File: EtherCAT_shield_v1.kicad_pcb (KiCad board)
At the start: 2 copper layers, 73.7 x 81.3 mm, 69 parts, among them J1 RJ45-PULSETRANS, J2 RJ45-PULSETRANS, P1 CONN_02X10, P2 CONN_02X19, P3 CONN_02X19, U1 LAN9252, U2 24LC00, Y1 Crystal_GND24

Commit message: ロゴ追加した
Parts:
- added G***: LOGO, EtherCAT_Logo:EtherCAT_900dpi, F.Cu at (102.0, 65.0)
- moved D1 11.7 mm to (109.8, 74.0)
- moved D2 11.7 mm to (109.8, 77.0)
- moved R1 11.7 mm to (106.8, 74.0)
- moved R2 11.7 mm to (106.8, 77.0)

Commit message: 進捗
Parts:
- U2: footprint Housings_SOIC:SOIC-8_3.9x4.9mm_Pitch1.27mm -> Housings_DIP:DIP-8_W7.62mm_Socket_LongPads
- moved C6 48.7 mm to (137.4, 91.2), turned to 270 degrees
- moved C7 44.7 mm to (140.0, 86.2)
- moved C10 20.0 mm to (162.3, 71.4)
- moved C8 20.0 mm to (162.3, 74.2)
- moved C9 20.0 mm to (162.3, 72.8)
- moved C25 11.6 mm to (145.9, 78.9), turned to 0 degrees
- moved C12 11.6 mm to (133.8, 94.8)
- moved C13 11.6 mm to (136.7, 93.5)
- moved C14 11.6 mm to (133.8, 93.5)
- moved C15 11.6 mm to (136.7, 94.8)
- moved U2 10.7 mm to (144.6, 89.0), turned to 90 degrees
- moved R22 10.4 mm to (153.7, 72.2), turned to 90 degrees
- moved R24 9.55 mm to (149.0, 72.0), turned to 270 degrees
- moved R23 9.36 mm to (155.3, 72.2), turned to 90 degrees
- moved R19 9.31 mm to (150.2, 78.4), turned to 270 degrees
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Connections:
- J1 pad 11: Net-(J1-Pad11) -> (no net)
- J1 pad 12: Net-(J1-Pad12) -> (no net)
- J1 pad 13: GND -> GNDPWR
- J1 pad 14: GND -> GNDPWR
- J1 pad 8: GND -> GNDPWR
- J2 pad 11: Net-(J2-Pad11) -> (no net)
- J2 pad 12: Net-(J2-Pad12) -> (no net)
- J2 pad 13: GND -> GNDPWR
- J2 pad 14: GND -> GNDPWR
- J2 pad 8: GND -> GNDPWR
- P2 pad 10: Net-(P2-Pad10) -> (no net)
- P2 pad 11: Net-(P2-Pad11) -> (no net)
- P2 pad 13: Net-(P2-Pad13) -> (no net)
- P2 pad 14: Net-(P2-Pad14) -> (no net)
- P2 pad 15: Net-(P2-Pad15) -> (no net)
- P2 pad 17: Net-(P2-Pad17) -> (no net)
- P2 pad 18: Net-(P2-Pad18) -> (no net)
- P2 pad 2: Net-(P2-Pad2) -> (no net)
- P2 pad 21: Net-(P2-Pad21) -> (no net)
- P2 pad 23: Net-(P2-Pad23) -> (no net)
- P2 pad 24: Net-(P2-Pad24) -> (no net)
- P2 pad 25: Net-(P2-Pad25) -> (no net)
- P2 pad 26: Net-(P2-Pad26) -> (no net)
- P2 pad 27: Net-(P2-Pad27) -> (no net)
- P2 pad 28: Net-(P2-Pad28) -> (no net)
- P2 pad 29: Net-(P2-Pad29) -> (no net)
- P2 pad 3: Net-(P2-Pad3) -> (no net)
- P2 pad 30: Net-(P2-Pad30) -> (no net)
- P2 pad 31: Net-(P2-Pad31) -> (no net)
- P2 pad 32: Net-(P2-Pad32) -> (no net)
- P2 pad 33: Net-(P2-Pad33) -> (no net)
- P2 pad 34: Net-(P2-Pad34) -> (no net)
- P2 pad 35: Net-(P2-Pad35) -> (no net)
- P2 pad 36: Net-(P2-Pad36) -> (no net)
- P2 pad 37: Net-(P2-Pad37) -> (no net)
- P2 pad 38: Net-(P2-Pad38) -> (no net)
- P2 pad 4: Net-(P2-Pad4) -> (no net)
- P2 pad 5: Net-(P2-Pad5) -> (no net)
- P2 pad 6: Net-(P2-Pad6) -> (no net)
- P2 pad 7: Net-(P2-Pad7) -> (no net)
- P2 pad 9: Net-(P2-Pad9) -> (no net)
- P3 pad 10: Net-(P3-Pad10) -> (no net)
- P3 pad 11: Net-(P3-Pad11) -> (no net)
- P3 pad 12: Net-(P3-Pad12) -> (no net)
- P3 pad 13: Net-(P3-Pad13) -> (no net)
- P3 pad 14: Net-(P3-Pad14) -> (no net)
- P3 pad 15: Net-(P3-Pad15) -> (no net)
- P3 pad 16: Net-(P3-Pad16) -> (no net)
- P3 pad 18: Net-(P3-Pad18) -> (no net)
- P3 pad 19: Net-(P3-Pad19) -> (no net)
- P3 pad 2: Net-(P3-Pad2) -> (no net)
- P3 pad 21: Net-(P3-Pad21) -> (no net)
- P3 pad 23: Net-(P3-Pad23) -> (no net)
- P3 pad 24: Net-(P3-Pad24) -> (no net)
- P3 pad 25: Net-(P3-Pad25) -> (no net)
- P3 pad 26: Net-(P3-Pad26) -> (no net)
- P3 pad 27: Net-(P3-Pad27) -> (no net)
- P3 pad 28: Net-(P3-Pad28) -> (no net)
- P3 pad 29: Net-(P3-Pad29) -> (no net)
- P3 pad 3: Net-(P3-Pad3) -> (no net)
- P3 pad 30: Net-(P3-Pad30) -> (no net)
- P3 pad 31: Net-(P3-Pad31) -> (no net)
- P3 pad 33: Net-(P3-Pad33) -> (no net)
- P3 pad 34: Net-(P3-Pad34) -> (no net)
- P3 pad 35: Net-(P3-Pad35) -> (no net)
- P3 pad 36: Net-(P3-Pad36) -> (no net)
- P3 pad 37: Net-(P3-Pad37) -> (no net)
- P3 pad 38: Net-(P3-Pad38) -> (no net)
- P3 pad 4: Net-(P3-Pad4) -> (no net)
- P3 pad 5: Net-(P3-Pad5) -> (no net)
- P3 pad 6: Net-(P3-Pad6) -> (no net)
- P3 pad 7: Net-(P3-Pad7) -> (no net)
- P3 pad 8: Net-(P3-Pad8) -> (no net)
- R23 pad 2: Net-(D3-Pad1) -> +3V3
- U1 pad 12: Net-(U1-Pad12) -> (no net)
- U1 pad 18: Net-(U1-Pad18) -> (no net)
- U1 pad 25: Net-(U1-Pad25) -> (no net)
- U1 pad 3: Net-(U1-Pad3) -> (no net)
- U1 pad 34: Net-(U1-Pad34) -> (no net)
- U1 pad 35: Net-(U1-Pad35) -> (no net)
- U1 pad 44: /LAN9252/IRQ -> (no net)
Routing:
- net Net-(P1-Pad9): track 2.25 -> 55.5 mm, vias 1 -> 2
- net +3V3: track 0.00 -> 52.8 mm, vias 0 -> 2
- net GNDPWR: track 0.00 -> 51.9 mm
- net Net-(P1-Pad7): track 0.00 -> 51.3 mm, vias 0 -> 1
- net Net-(P1-Pad5): track 0.00 -> 48.7 mm, vias 0 -> 1
- net Net-(P1-Pad16): track 0.00 -> 47.0 mm, vias 0 -> 1
- net Net-(P1-Pad3): track 0.00 -> 45.1 mm
- net Net-(P1-Pad17): track 0.00 -> 44.2 mm
- net Net-(P1-Pad15): track 0.00 -> 43.7 mm
- net Net-(P1-Pad13): track 0.00 -> 42.7 mm
- net Net-(P1-Pad4): track 0.00 -> 41.9 mm, vias 0 -> 1
- net Net-(P1-Pad11): track 0.00 -> 41.8 mm, vias 0 -> 1
- net Net-(P1-Pad14): track 0.00 -> 40.6 mm
- net Net-(P1-Pad6): track 0.00 -> 39.6 mm
- net Net-(P1-Pad8): track 0.00 -> 39.1 mm, vias 0 -> 1
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- added copper zone on B.Cu, net GND
- added copper zone on F.Cu, net GND

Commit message: 進捗
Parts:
- C5, C6, C7, C8, C9, R18: moved to B.Cu
- moved C10 37.4 mm to (126.5, 82.2), turned to 90 degrees
- moved C9 36.8 mm to (128.4, 87.2)
- moved C8 34.7 mm to (131.1, 89.4), turned to 90 degrees
- moved C12 13.2 mm to (129.9, 82.2), turned to 90 degrees
- moved C14 12.4 mm to (128.5, 82.2), turned to 90 degrees
- moved C15 9.71 mm to (138.1, 85.2), turned to 180 degrees
- moved R21 9.11 mm to (123.4, 83.8), turned to 90 degrees
- moved R12 7.50 mm to (125.0, 83.8), turned to 90 degrees
- moved C1 6.91 mm to (121.9, 83.8), turned to 90 degrees
- moved C13 5.73 mm to (132.6, 89.4), turned to 90 degrees
- moved R4 5.53 mm to (120.4, 83.8), turned to 270 degrees
- moved R2 3.15 mm to (108.6, 75.5), turned to 0 degrees
- moved R1 3.05 mm to (108.6, 72.5), turned to 0 degrees
- moved R18 3.01 mm to (128.1, 84.4), turned to 0 degrees
- moved D2 2.95 mm to (111.6, 75.5), turned to 180 degrees
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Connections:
- P2 pad 21: (no net) -> /LAN9252/IRQ
- P2 pad 23: (no net) -> /LAN9252/~RST
- P2 pad 25: (no net) -> Net-(P2-Pad25)
- P2 pad 27: (no net) -> Net-(P2-Pad27)
- P2 pad 6: (no net) -> +5V
- U1 pad 18: (no net) -> Net-(P2-Pad27)
- U1 pad 34: (no net) -> Net-(P2-Pad25)
- U1 pad 44: (no net) -> /LAN9252/IRQ
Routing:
- net GND: track 143.2 -> 299.6 mm, vias 16 -> 33
- net +3V3: track 52.8 -> 186.8 mm, vias 2 -> 9
- net /LAN9252/IRQ: track 0.00 -> 63.3 mm, vias 0 -> 1
- net /LAN9252/~RST: track 0.00 -> 55.0 mm, vias 0 -> 1
- net Net-(P2-Pad27): track 0.00 -> 44.2 mm, vias 0 -> 2
- net Net-(P1-Pad16): track 47.0 -> 3.96 mm, vias 1 -> 0
- net Net-(P1-Pad4): track 41.9 -> 3.47 mm, vias 1 -> 0
- net Net-(P3-Pad17): track 3.35 -> 41.4 mm
- net Net-(C12-Pad1): track 0.00 -> 37.4 mm, vias 0 -> 3
- net Net-(P1-Pad14): track 40.6 -> 3.26 mm
- net Net-(P1-Pad6): track 39.6 -> 3.49 mm
- net Net-(P1-Pad8): track 39.1 -> 3.53 mm, vias 1 -> 0
- net Net-(P1-Pad12): track 39.0 -> 3.69 mm, vias 1 -> 0
- net Net-(P1-Pad10): track 38.4 -> 4.15 mm, vias 1 -> 0
- net Net-(P1-Pad3): track 45.1 -> 10.9 mm
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
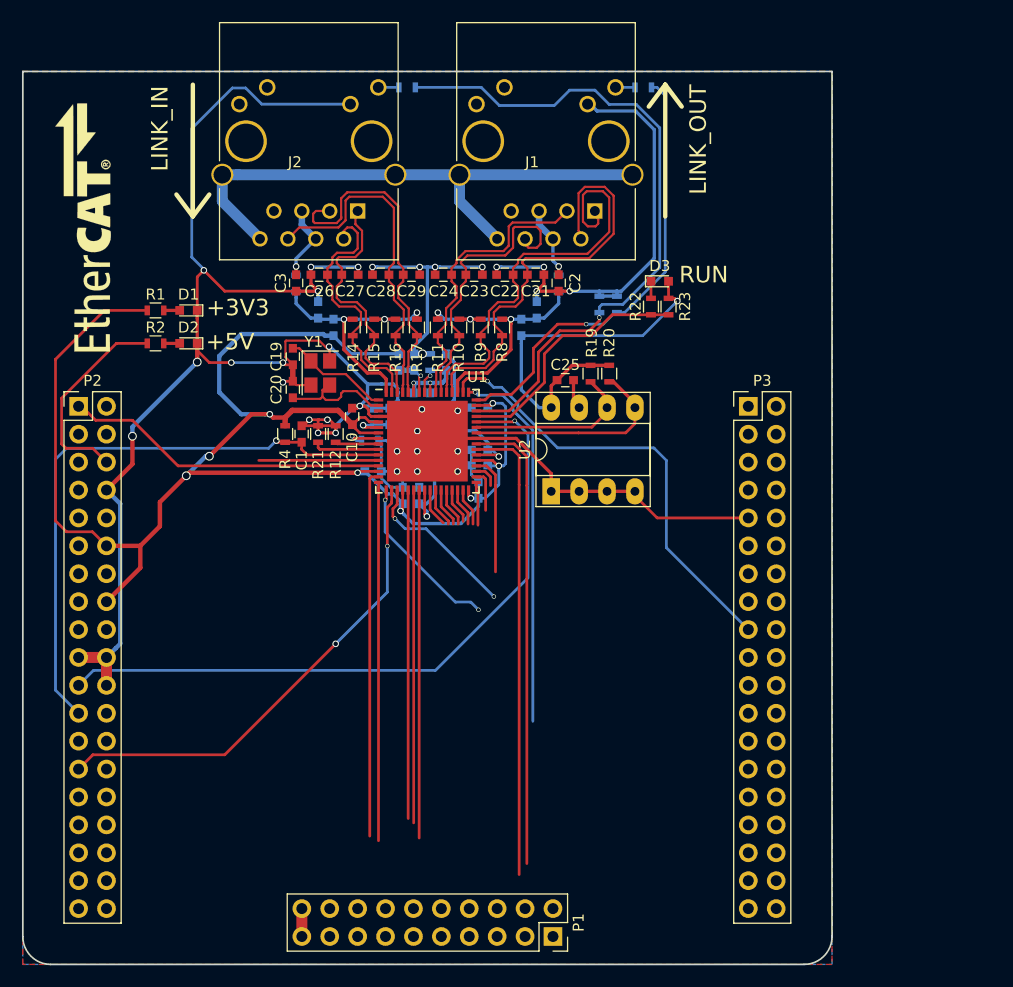
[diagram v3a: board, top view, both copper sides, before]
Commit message: LED変更，再アノテーション
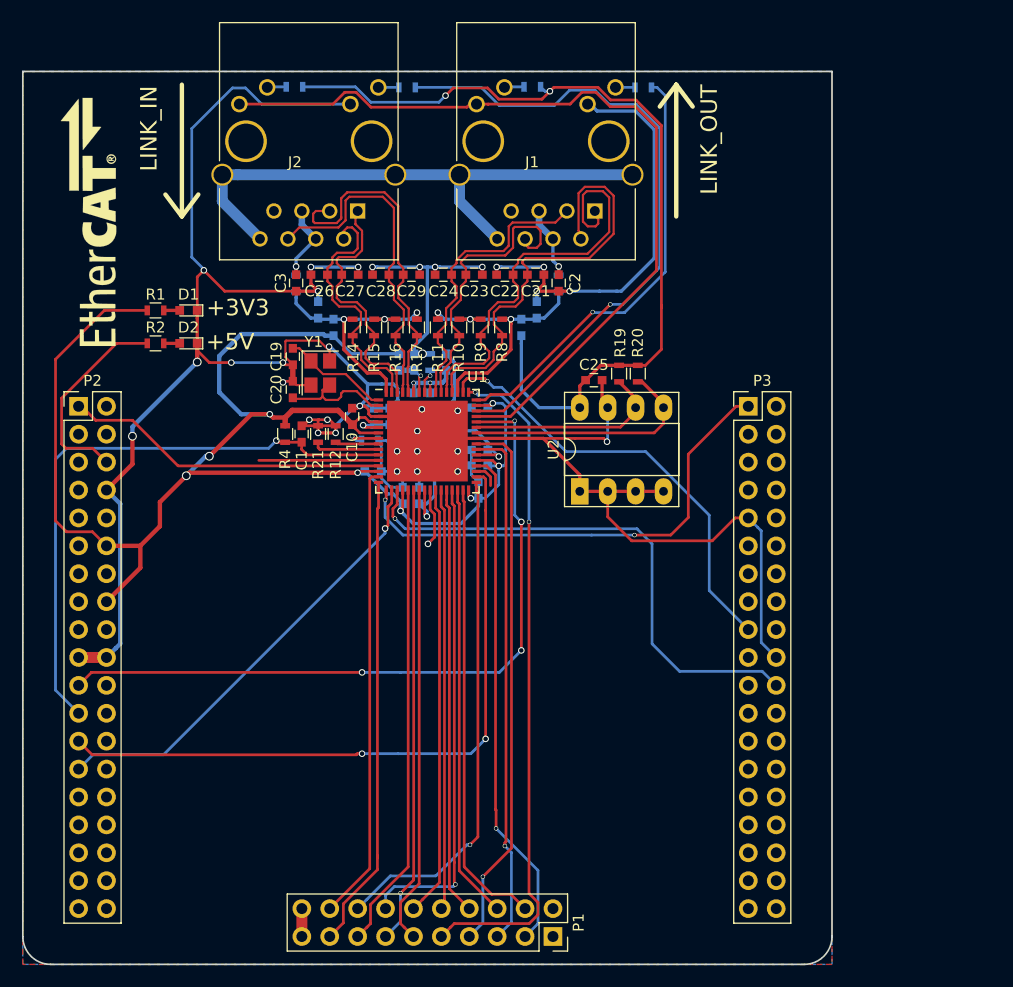
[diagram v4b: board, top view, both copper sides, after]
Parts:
- removed D3: LED, LEDs:LED_0603
- removed R24, R25: 10k, Resistors_SMD:R_0603
- R22: value 1k -> 330; moved to B.Cu
- R23: value 10k -> 330; moved to B.Cu
- moved R23 39.5 mm to (121.2, 52.2), turned to 180 degrees
- moved R22 22.7 mm to (142.9, 52.2), turned to 180 degrees
- moved R19 2.60 mm to (150.8, 78.3)
- moved C25 2.60 mm to (148.5, 78.9)
- moved R20 2.60 mm to (152.5, 78.3)
- moved U2 2.60 mm to (147.2, 89.0)
- moved G*** 0.71 mm to (102.5, 64.5)
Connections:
- net Net-(P2-Pad1) renamed SIO1
- net Net-(P3-Pad1) renamed SIO0
- net Net-(P3-Pad17) renamed ~SCS
- net Net-(P3-Pad22) renamed SCK
- J1 pad 11: (no net) -> Net-(J1-Pad11)
- J1 pad 12: (no net) -> /LAN9252/RUNLED
- J2 pad 11: (no net) -> Net-(J2-Pad11)
- J2 pad 12: (no net) -> /LAN9252/RUNLED
- R22 pad 1: Net-(R22-Pad1) -> +3V3
- R22 pad 2: Net-(D3-Pad1) -> Net-(J1-Pad11)
- R23 pad 1: Net-(R22-Pad1) -> +3V3
- R23 pad 2: +3V3 -> Net-(J2-Pad11)
- U1 pad 45: Net-(R22-Pad1) -> /LAN9252/RUNLED
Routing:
- net /LAN9252/RUNLED: track 0.00 -> 75.8 mm
- net Net-(P2-Pad25): track 3.79 -> 62.8 mm, vias 0 -> 2
- net +3V3: track 186.8 -> 231.9 mm, vias 9 -> 10
- net Net-(P1-Pad16): track 3.96 -> 46.0 mm, vias 0 -> 1
- net Net-(P1-Pad14): track 3.26 -> 44.1 mm, vias 0 -> 1
- net Net-(P1-Pad4): track 3.47 -> 41.5 mm
- net Net-(P1-Pad6): track 3.49 -> 39.6 mm
- net Net-(P1-Pad12): track 3.69 -> 39.3 mm
- net Net-(P1-Pad8): track 3.53 -> 39.0 mm
- net Net-(P1-Pad3): track 10.9 -> 46.2 mm, vias 0 -> 1
- net SCK: track 14.8 -> 49.2 mm, vias 2 -> 1
- net Net-(P1-Pad10): track 4.15 -> 38.3 mm
- net GND: track 299.6 -> 331.8 mm, vias 33 -> 34
- net SIO0: track 15.3 -> 44.5 mm
- net Net-(P1-Pad9): track 34.3 -> 61.4 mm, vias 1 -> 2
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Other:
- board text removed: "RUN"

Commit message: GPIOのLED並べた 実質完成
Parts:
- added D10: LED, LEDs:LED_0603, F.Cu at (121.9, 122.6)
- added D11: LED, LEDs:LED_0603, F.Cu at (144.8, 104.8)
- added D12: LED, LEDs:LED_0603, F.Cu at (144.8, 107.3)
- added D13: LED, LEDs:LED_0603, F.Cu at (144.8, 109.9)
- added D14: LED, LEDs:LED_0603, F.Cu at (144.8, 112.4)
- added D15: LED, LEDs:LED_0603, F.Cu at (144.8, 114.9)
- added D16: LED, LEDs:LED_0603, F.Cu at (144.8, 117.5)
- added D17: LED, LEDs:LED_0603, F.Cu at (144.8, 120.0)
- added D18: LED, LEDs:LED_0603, F.Cu at (144.8, 122.6)
- added D3: LED, LEDs:LED_0603, F.Cu at (121.9, 104.8)
- added D4: LED, LEDs:LED_0603, F.Cu at (121.9, 107.3)
- added D5: LED, LEDs:LED_0603, F.Cu at (121.9, 109.9)
- added D6: LED, LEDs:LED_0603, F.Cu at (121.9, 112.4)
- added D7: LED, LEDs:LED_0603, F.Cu at (121.9, 114.9)
- added D8: LED, LEDs:LED_0603, F.Cu at (121.9, 117.5)
- added D9: LED, LEDs:LED_0603, F.Cu at (121.9, 120.0)
- added J3: GS3, Connect:GS3, B.Cu at (159.0, 101.7)
- added J4: GS3, Connect:GS3, B.Cu at (159.0, 109.1)
- added J5: GS3, Connect:GS3, F.Cu at (109.5, 82.5)
- added J6: GS3, Connect:GS3, B.Cu at (152.0, 94.7)
- added J7: GS2, Connect:GS2, B.Cu at (143.7, 94.3)
- added J8: GS2, Connect:GS2, B.Cu at (143.7, 96.7)
- added R24: 1k, Resistors_SMD:R_0603, B.Cu at (126.4, 104.8)
- added R25: 1k, Resistors_SMD:R_0603, B.Cu at (126.4, 107.3)
- added R26: 1k, Resistors_SMD:R_0603, B.Cu at (126.2, 109.9)
- added R27: 1k, Resistors_SMD:R_0603, B.Cu at (126.4, 112.4)
- added R28: 1k, Resistors_SMD:R_0603, B.Cu at (126.4, 114.9)
- added R29: 1k, Resistors_SMD:R_0603, B.Cu at (126.4, 117.5)
- added R30: 1k, Resistors_SMD:R_0603, B.Cu at (126.2, 120.0)
- added R31: 1k, Resistors_SMD:R_0603, B.Cu at (126.4, 122.6)
- added R32: 1k, Resistors_SMD:R_0603, B.Cu at (141.5, 104.8)
- added R33: 1k, Resistors_SMD:R_0603, B.Cu at (141.5, 107.3)
- added R34: 1k, Resistors_SMD:R_0603, B.Cu at (141.5, 109.9)
- added R35: 1k, Resistors_SMD:R_0603, B.Cu at (141.5, 112.4)
- added R36: 1k, Resistors_SMD:R_0603, B.Cu at (141.5, 114.9)
- added R37: 1k, Resistors_SMD:R_0603, B.Cu at (141.5, 117.5)
- added R38: 1k, Resistors_SMD:R_0603, B.Cu at (141.5, 120.0)
- added R39: 1k, Resistors_SMD:R_0603, B.Cu at (141.5, 122.6)
- moved R1 51.2 mm to (113.6, 123.5), turned to 180 degrees
- moved R2 51.0 mm to (113.6, 126.3), turned to 180 degrees
- moved D1 51.0 mm to (110.6, 123.5), turned to 0 degrees
- moved D2 50.8 mm to (110.6, 126.3), turned to 0 degrees
- moved P1 13.5 mm to (132.1, 125.1), turned to 180 degrees
- moved C25 3.11 mm to (148.2, 75.8)
- moved R19 3.11 mm to (150.5, 75.2)
- moved R20 3.11 mm to (152.2, 75.2)
- moved U2 3.11 mm to (146.9, 85.9)
- turned R23 to 0 degrees
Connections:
- net /LAN9252/IRQ renamed LAN9252_IRQ
- net /LAN9252/~RST renamed LAN9252_RST
- net Net-(P1-Pad10) renamed GPIO12
- net Net-(P1-Pad12) renamed GPIO11
- net Net-(P1-Pad14) renamed GPIO10
- net Net-(P1-Pad16) renamed GPIO9
- net Net-(P1-Pad18) renamed GPIO8
- net Net-(P1-Pad4) renamed GPIO15
- net Net-(P1-Pad6) renamed GPIO14
- net Net-(P1-Pad8) renamed GPIO13
- net Net-(P2-Pad25) renamed SYNC0
- net Net-(P2-Pad27) renamed SYNC1
- P1 pad 11: Net-(P1-Pad11) -> GPIO3
- P1 pad 13: Net-(P1-Pad13) -> GPIO2
- P1 pad 15: Net-(P1-Pad15) -> GPIO1
- P1 pad 17: Net-(P1-Pad17) -> GPIO0
- P1 pad 3: Net-(P1-Pad3) -> GPIO7
- P1 pad 5: Net-(P1-Pad5) -> GPIO6
- P1 pad 7: Net-(P1-Pad7) -> GPIO5
- P1 pad 9: Net-(P1-Pad9) -> GPIO4
- P2 pad 1: SIO1 -> PC10
- P2 pad 18: (no net) -> +5V
- P2 pad 34: (no net) -> PB0
- P2 pad 6: +5V -> (no net)
- P3 pad 1: SIO0 -> PC9
- P3 pad 13: (no net) -> PA6
- P3 pad 15: (no net) -> PA7
- P3 pad 17: ~SCS -> PB6
- P3 pad 18: (no net) -> PB11
- P3 pad 22: SCK -> PB2
- P3 pad 24: (no net) -> PB1
- P3 pad 25: (no net) -> PB10
- R23 pad 1: +3V3 -> Net-(J2-Pad11)
- R23 pad 2: Net-(J2-Pad11) -> +3V3
- U1 pad 12: (no net) -> SIO2
- U1 pad 16: Net-(P1-Pad17) -> GPIO7
- U1 pad 21: Net-(P1-Pad15) -> GPIO6
- U1 pad 22: Net-(P1-Pad13) -> GPIO5
- U1 pad 23: Net-(P1-Pad11) -> GPIO4
- U1 pad 35: (no net) -> SIO3
- U1 pad 36: Net-(P1-Pad3) -> GPIO0
- U1 pad 39: Net-(P1-Pad5) -> GPIO1
- U1 pad 40: Net-(P1-Pad7) -> GPIO2
- U1 pad 49: Net-(P1-Pad9) -> GPIO3
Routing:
- net GND: track 331.8 -> 470.4 mm, vias 34 -> 40
- net Net-(P1-Pad9): track 61.4 -> 0.00 mm, vias 2 -> 0
- net GPIO3: track 0.00 -> 51.1 mm, vias 0 -> 3
- net PB0: track 0.00 -> 50.6 mm, vias 0 -> 1
- net Net-(P1-Pad7): track 49.2 -> 0.00 mm, vias 1 -> 0
- net Net-(P1-Pad5): track 47.6 -> 0.00 mm, vias 1 -> 0
- net Net-(P1-Pad3): track 46.2 -> 0.00 mm, vias 1 -> 0
- net Net-(P1-Pad17): track 43.4 -> 0.00 mm
- net Net-(P1-Pad15): track 42.5 -> 0.00 mm
- net GPIO2: track 0.00 -> 42.3 mm, vias 0 -> 1
- net Net-(P1-Pad11): track 41.8 -> 0.00 mm
- net Net-(P1-Pad13): track 41.7 -> 0.00 mm, vias 1 -> 0
- net GPIO7: track 0.00 -> 40.8 mm
- net +5V: track 18.8 -> 57.7 mm, vias 0 -> 1
- net GPIO1: track 0.00 -> 38.7 mm, vias 0 -> 1
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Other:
- outline, holes or cut-outs redrawn
- board text added: "@yuqlid"
- board text added: "EEPROM"
- board text added: "EtherCAT_Board ver1.0"
- board text added: "F446"
- board text added: "GND"
- board text added: "GPIO0"
- board text added: "GPIO1"
- board text added: "GPIO10"
- board text added: "GPIO11"
- board text added: "GPIO12"
- board text added: "GPIO13"
- board text added: "GPIO14"
- board text added: "GPIO15"
- board text added: "GPIO2"
- board text added: "GPIO3"
- board text added: "GPIO4"
- board text added: "GPIO5"
- board text added: "GPIO6"
- board text added: "GPIO7"
- board text added: "GPIO8"
- board text added: "GPIO9"
- board text added: "L476"
- board text added: "Nucleo-64"
